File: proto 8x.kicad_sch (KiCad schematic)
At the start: 22 parts, among them J1 AVR-ISP-6, Q1 DSS60601MZ4-13, SW1 SW_Push, U1 ATmega32U4-MU, U2 PRTR5V0U2X, Y1 16MHz

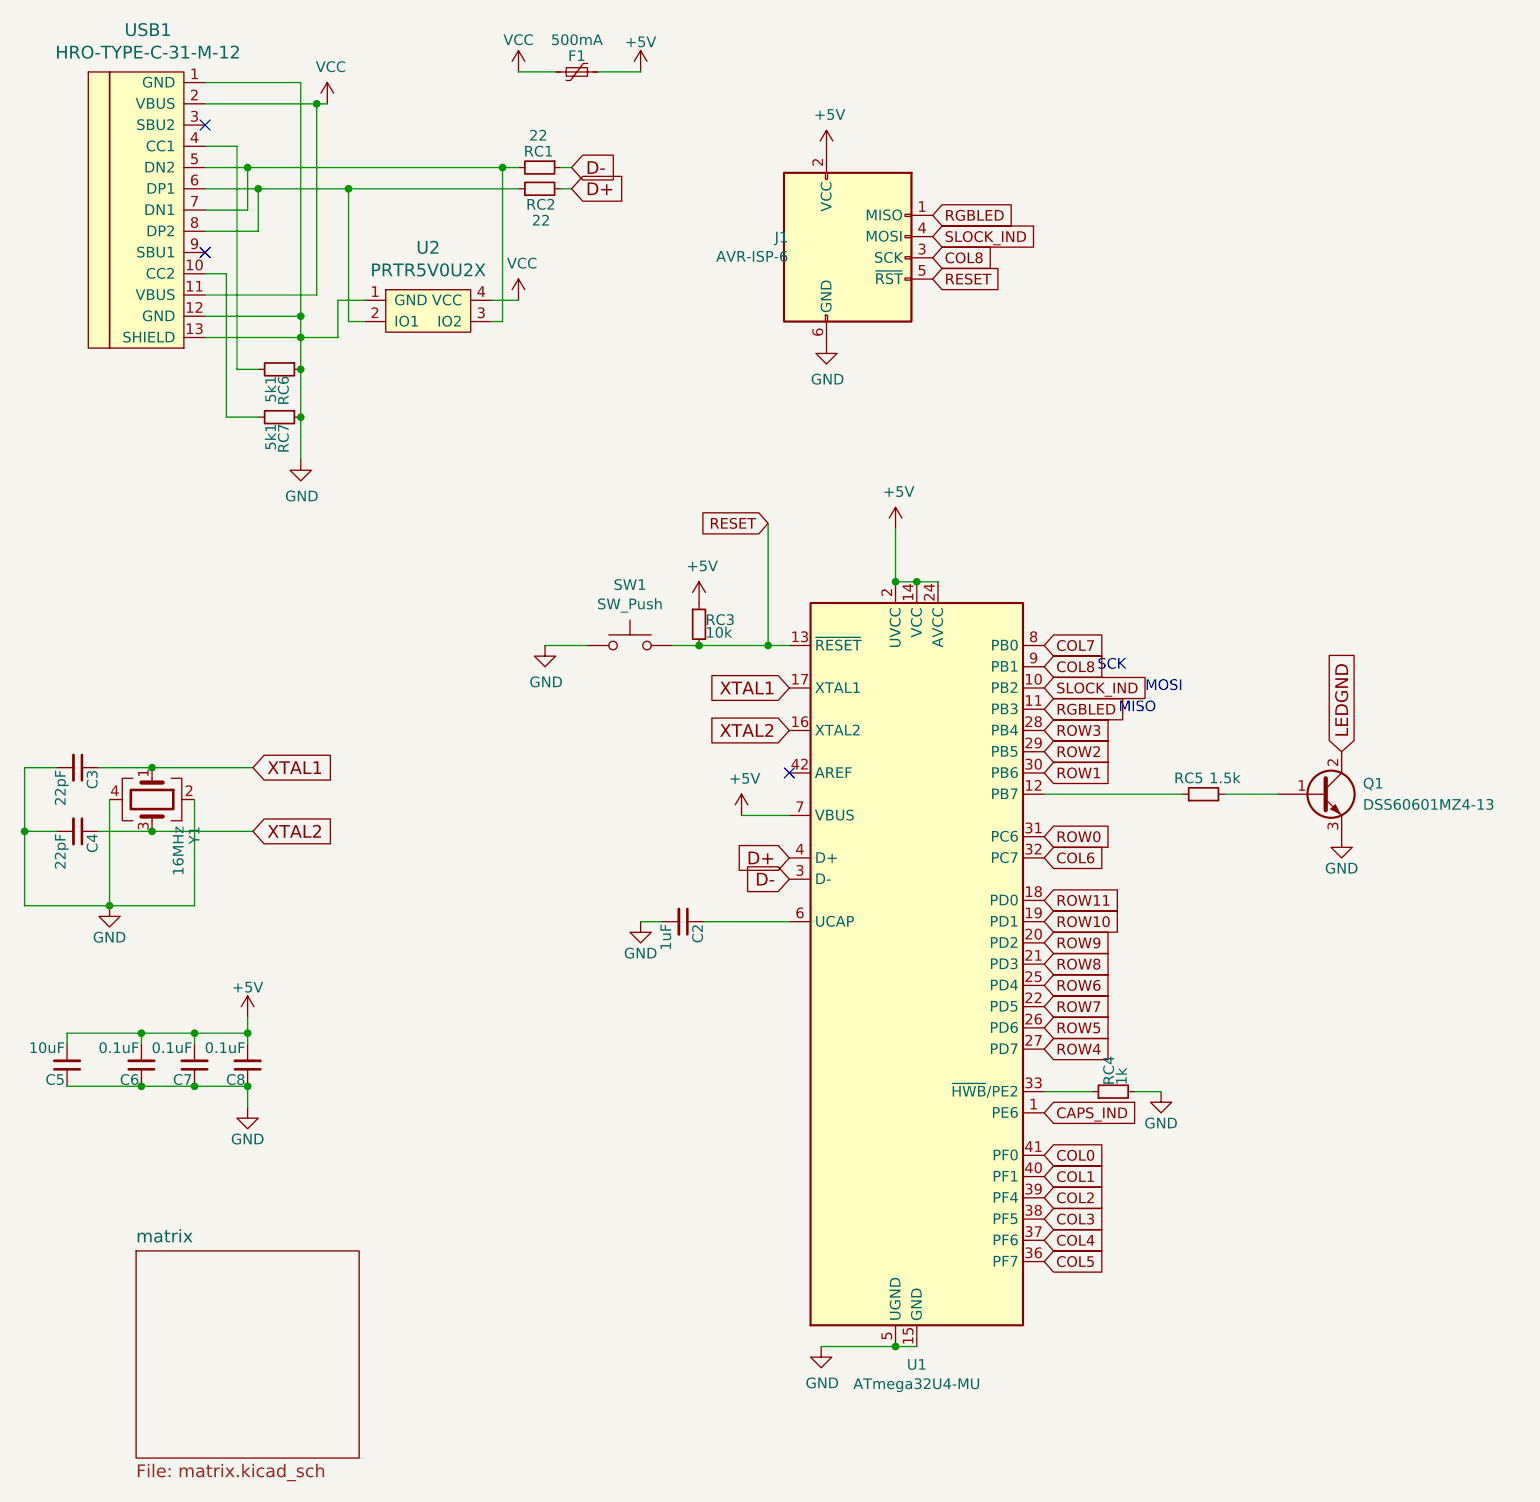
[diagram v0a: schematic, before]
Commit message: move f1 + many split layout to complex version, add more board ocmponents
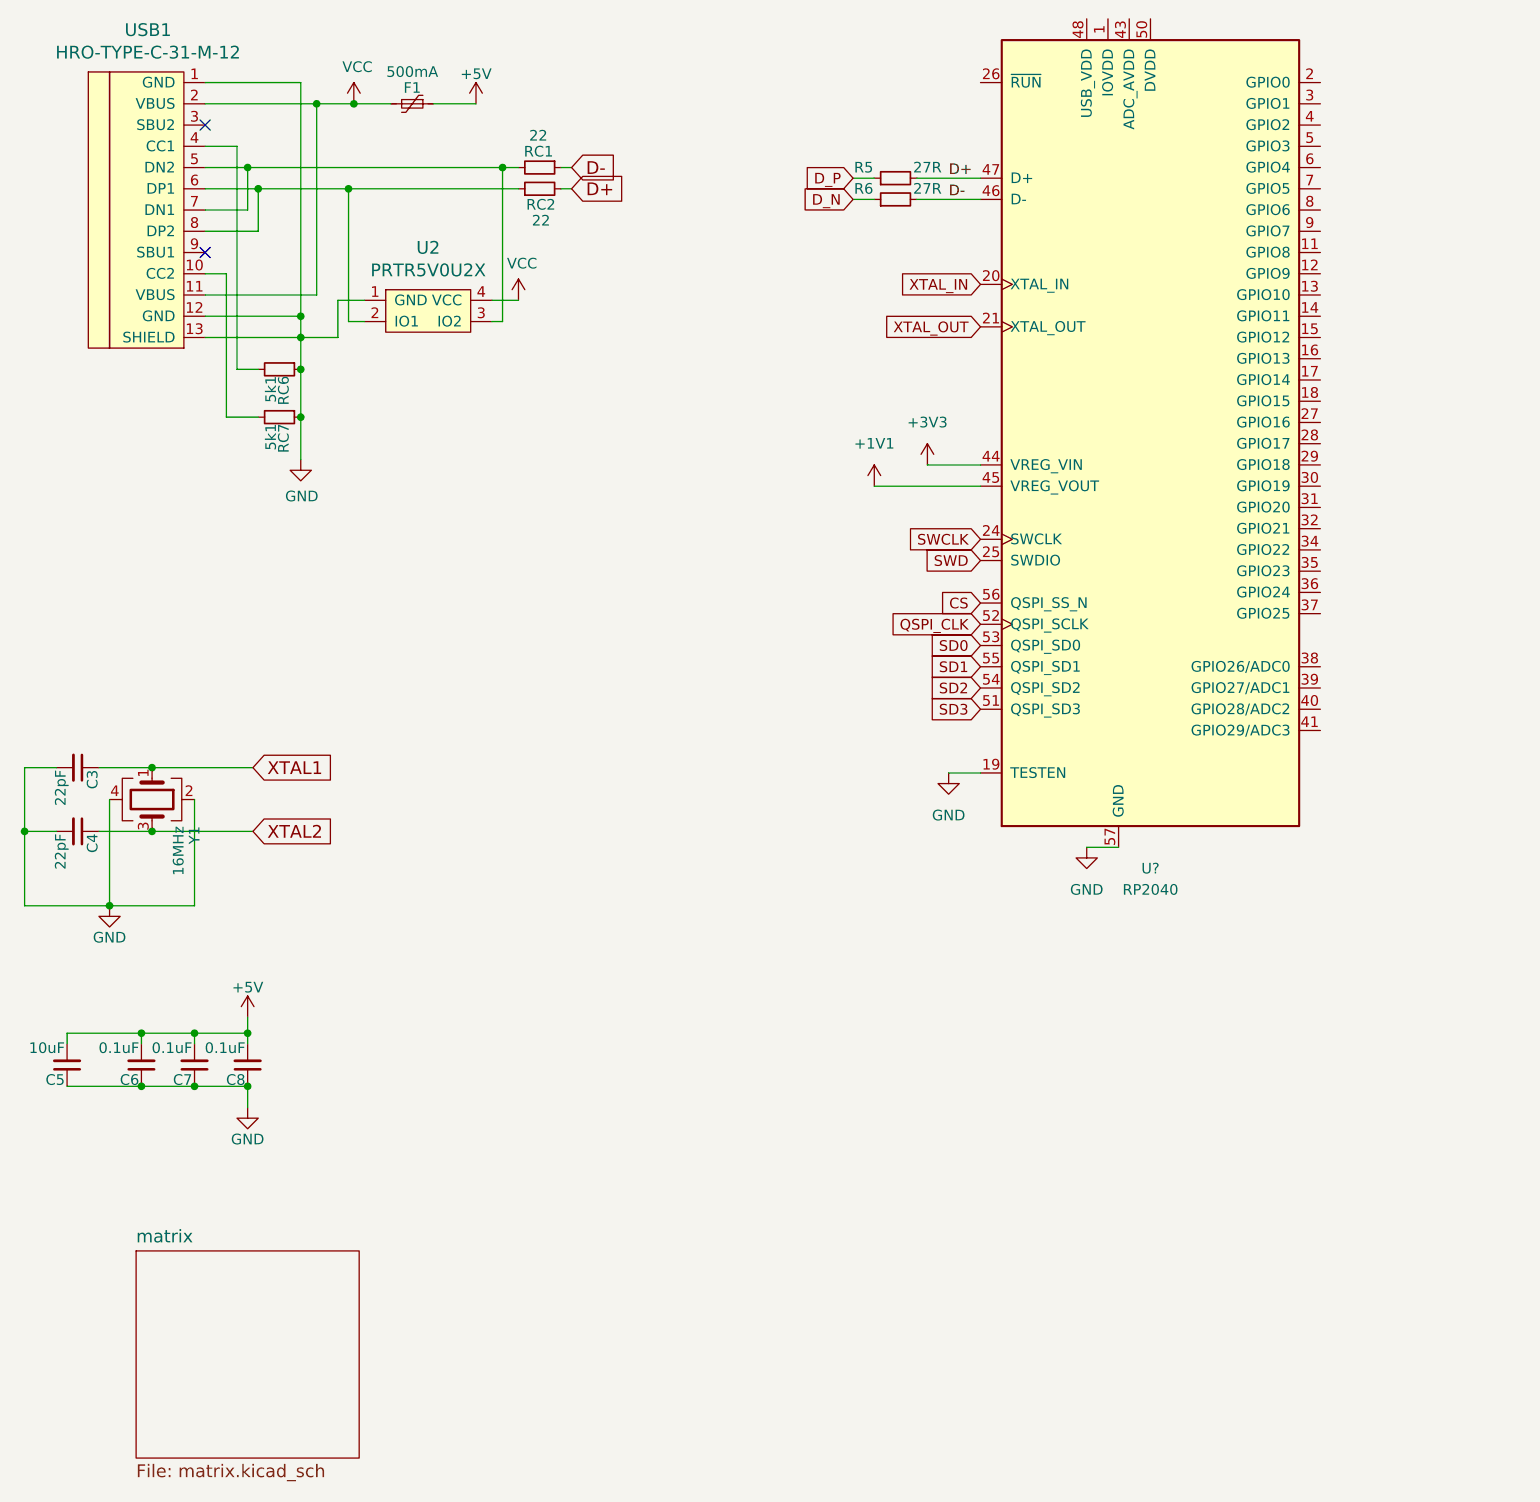
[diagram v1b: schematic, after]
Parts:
- removed C2: 1uF, locallib:C_0603, symbol Device:C_Small
- removed J1: AVR-ISP-6, random-keyboard-parts:Reset_Pretty-Mask, symbol Connector:AVR-ISP-6
- removed Q1: DSS60601MZ4-13, TO_SOT_Packages_SMD:SOT-223-3_TabPin2, symbol Device:Q_NPN_BCE
- removed RC3: 10k, locallib:R_0603, symbol Device:R_Small
- removed RC4: 1k, locallib:R_0603, symbol Device:R_Small
- removed RC5: 1.5k, locallib:R_0603, symbol Device:R_Small
- removed SW1: SW_Push, random-keyboard-parts:SKQG-1155865, symbol Switch:SW_Push
- removed U1: ATmega32U4-MU, locallib:QFN-44-1EP_7x7mm_Pitch0.5mm, symbol MCU_Microchip_ATmega:ATmega32U4-MU
- added R5, R6: 27R, Resistor_SMD:R_0603_1608Metric, symbol Device:R_Small
- added U?: RP2040, Sleep-Lib:RP2040-QFN-56, symbol Sleep-lib:RP2040
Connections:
- net D+: now also R5.2, U?.47 (D+)
- net D-: now also R6.2, U?.46 (D-)
- net GND: now also U?.19 (TESTEN), U?.57 (GND)
- new net +1V1: U?.45 (VREG_VOUT)
- new net +3V3: U?.44 (VREG_VIN)
- new net CS: U?.56 (QSPI_SS_N)
- new net DVDD: U?.23 (DVDD), U?.50 (DVDD)
- new net D_N: R6.1
- new net D_P: R5.1
- new net IOVDD: U?.1 (IOVDD), U?.10 (IOVDD), U?.22 (IOVDD), U?.33 (IOVDD), U?.42 (IOVDD), U?.49 (IOVDD)
- new net QSPI_CLK: U?.52 (QSPI_SCLK)
- new net SD0: U?.53 (QSPI_SD0)
- new net SD1: U?.55 (QSPI_SD1)
- new net SD2: U?.54 (QSPI_SD2)
- new net SD3: U?.51 (QSPI_SD3)
- new net SWCLK: U?.24 (SWCLK)
- new net SWD: U?.25 (SWDIO)
- new net XTAL_IN: U?.20 (XTAL_IN)
- new net XTAL_OUT: U?.21 (XTAL_OUT)
- no-connect marks 3 -> 2
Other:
- note removed: "MISO"
- note removed: "MOSI"
- note removed: "SCK"
- moved on the sheet: F1
